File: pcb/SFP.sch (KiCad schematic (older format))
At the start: 13 parts, among them J1101 SFP_CONN

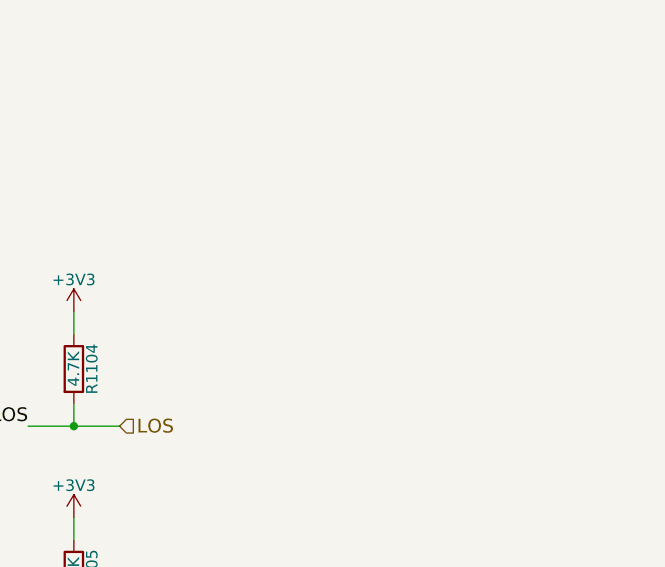
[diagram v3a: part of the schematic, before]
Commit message: Finished most of the routing, removed DDR-3
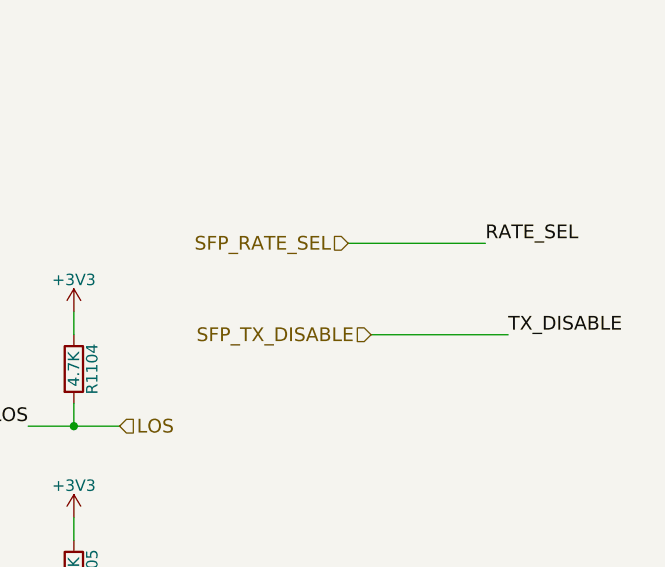
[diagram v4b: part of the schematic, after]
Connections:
- net RATE_SEL renamed SFP_RATE_SEL
- net TX_DISABLE renamed SFP_TX_DISABLE
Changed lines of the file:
@@
 $Descr A4 11693 8268
 encoding utf-8
-Sheet 11 13
+Sheet 9 11
 Title ""
 Date ""
@@
 $EndComp
 $Comp
-L GND #PWR0153
+L GND #PWR0138
 U 1 1 56515F98
 P 2700 3100
-F 0 "#PWR0153" H 2700 2850 50  0001 C CNN
+F 0 "#PWR0138" H 2700 2850 50  0001 C CNN
 F 1 "GND" H 2700 2950 50  0000 C CNN
 F 2 "" H 2700 3100 60  0000 C CNN
@@
 $EndComp
 $Comp
-L +3V3 #PWR0154
+L +3V3 #PWR0139
 U 1 1 56515FAF
 P 7900 1000
-F 0 "#PWR0154" H 7900 850 50  0001 C CNN
+F 0 "#PWR0139" H 7900 850 50  0001 C CNN
 F 1 "+3V3" H 7900 1140 50  0000 C CNN
 F 2 "" H 7900 1000 60  0000 C CNN
@@
 $EndComp
 $Comp
-L GND #PWR0155
+L GND #PWR0140
 U 1 1 56515FCB
 P 7900 1500
-F 0 "#PWR0155" H 7900 1250 50  0001 C CNN
+F 0 "#PWR0140" H 7900 1250 50  0001 C CNN
 F 1 "GND" H 7900 1350 50  0000 C CNN
 F 2 "" H 7900 1500 60  0000 C CNN
@@
 $EndComp
 $Comp
-L GND #PWR0156
+L GND #PWR0141
 U 1 1 565162BE
 P 7000 1500
-F 0 "#PWR0156" H 7000 1250 50  0001 C CNN
+F 0 "#PWR0141" H 7000 1250 50  0001 C CNN
 F 1 "GND" H 7000 1350 50  0000 C CNN
 F 2 "" H 7000 1500 60  0000 C CNN
@@
 $EndComp
 $Comp
-L GND #PWR0157
+L GND #PWR0142
 U 1 1 5651631D
 P 6700 2600
-F 0 "#PWR0157" H 6700 2350 50  0001 C CNN
+F 0 "#PWR0142" H 6700 2350 50  0001 C CNN
 F 1 "GND" H 6700 2450 50  0000 C CNN
 F 2 "" H 6700 2600 60  0000 C CNN
@@
 $EndComp
 $Comp
-L +3V3 #PWR0158
+L +3V3 #PWR0143
 U 1 1 56516349
 P 5700 800
-F 0 "#PWR0158" H 5700 650 50  0001 C CNN
+F 0 "#PWR0143" H 5700 650 50  0001 C CNN
 F 1 "+3V3" H 5700 940 50  0000 C CNN
 F 2 "" H 5700 800 60  0000 C CNN
@@
 $EndComp
 $Comp
-L +3V3 #PWR0159
+L +3V3 #PWR0144
 U 1 1 56516375
 P 5700 1900
-F 0 "#PWR0159" H 5700 1750 50  0001 C CNN
+F 0 "#PWR0144" H 5700 1750 50  0001 C CNN
 F 1 "+3V3" H 5700 2040 50  0000 C CNN
 F 2 "" H 5700 1900 60  0000 C CNN
@@
 $EndComp
 $Comp
-L +3V3 #PWR0160
+L +3V3 #PWR0145
 U 1 1 56516B32
 P 7500 3600
-F 0 "#PWR0160" H 7500 3450 50  0001 C CNN
+F 0 "#PWR0145" H 7500 3450 50  0001 C CNN
 F 1 "+3V3" H 7500 3740 50  0000 C CNN
 F 2 "" H 7500 3600 60  0000 C CNN
@@
 $EndComp
 $Comp
-L +3V3 #PWR0161
+L +3V3 #PWR0146
 U 1 1 56516C8D
 P 7500 4500
-F 0 "#PWR0161" H 7500 4350 50  0001 C CNN
+F 0 "#PWR0146" H 7500 4350 50  0001 C CNN
 F 1 "+3V3" H 7500 4640 50  0000 C CNN
 F 2 "" H 7500 4500 60  0000 C CNN
@@
 $EndComp
 $Comp
-L +3V3 #PWR0162
+L +3V3 #PWR0147
 U 1 1 56516D11
 P 5300 3600
-F 0 "#PWR0162" H 5300 3450 50  0001 C CNN
+F 0 "#PWR0147" H 5300 3450 50  0001 C CNN
 F 1 "+3V3" H 5300 3740 50  0000 C CNN
 F 2 "" H 5300 3600 60  0000 C CNN
@@
 $EndComp
 $Comp
-L +3V3 #PWR0163
+L +3V3 #PWR0148
 U 1 1 56516D21
 P 5300 4500
-F 0 "#PWR0163" H 5300 4350 50  0001 C CNN
+F 0 "#PWR0148" H 5300 4350 50  0001 C CNN
 F 1 "+3V3" H 5300 4640 50  0000 C CNN
 F 2 "" H 5300 4500 60  0000 C CNN
@@
 $EndComp
 $Comp
-L +3V3 #PWR0164
+L +3V3 #PWR0149
 U 1 1 56516DA0
 P 5300 5400
-F 0 "#PWR0164" H 5300 5250 50  0001 C CNN
+F 0 "#PWR0149" H 5300 5250 50  0001 C CNN
 F 1 "+3V3" H 5300 5540 50  0000 C CNN
 F 2 "" H 5300 5400 60  0000 C CNN
@@
 Text HLabel 7700 6000 2    60   Input ~ 0
 SFP_TX_N
+Wire Wire Line
+	8700 3300 9300 3300
+Text HLabel 8700 3300 0    60   Input ~ 0
+SFP_RATE_SEL
+Text Label 9300 3300 0    60   ~ 0
+RATE_SEL
+Text Label 9400 3700 0    60   ~ 0
+TX_DISABLE
+Wire Wire Line
+	9400 3700 8800 3700
+Text HLabel 8800 3700 0    60   Input ~ 0
+SFP_TX_DISABLE
 $EndSCHEMATC

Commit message: Pending final check
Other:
- note added: "SFP has internal AC coupling caps"
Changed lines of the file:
@@
 $EndComp
 $Comp
-L GND #PWR0138
+L GND #PWR0139
 U 1 1 56515F98
 P 2700 3100
-F 0 "#PWR0138" H 2700 2850 50  0001 C CNN
+F 0 "#PWR0139" H 2700 2850 50  0001 C CNN
 F 1 "GND" H 2700 2950 50  0000 C CNN
 F 2 "" H 2700 3100 60  0000 C CNN
@@
 $EndComp
 $Comp
-L +3V3 #PWR0139
+L +3V3 #PWR0140
 U 1 1 56515FAF
 P 7900 1000
-F 0 "#PWR0139" H 7900 850 50  0001 C CNN
+F 0 "#PWR0140" H 7900 850 50  0001 C CNN
 F 1 "+3V3" H 7900 1140 50  0000 C CNN
 F 2 "" H 7900 1000 60  0000 C CNN
@@
 $EndComp
 $Comp
-L GND #PWR0140
+L GND #PWR0141
 U 1 1 56515FCB
 P 7900 1500
-F 0 "#PWR0140" H 7900 1250 50  0001 C CNN
+F 0 "#PWR0141" H 7900 1250 50  0001 C CNN
 F 1 "GND" H 7900 1350 50  0000 C CNN
 F 2 "" H 7900 1500 60  0000 C CNN
@@
 $EndComp
 $Comp
-L GND #PWR0141
+L GND #PWR0142
 U 1 1 565162BE
 P 7000 1500
-F 0 "#PWR0141" H 7000 1250 50  0001 C CNN
+F 0 "#PWR0142" H 7000 1250 50  0001 C CNN
 F 1 "GND" H 7000 1350 50  0000 C CNN
 F 2 "" H 7000 1500 60  0000 C CNN
@@
 $EndComp
 $Comp
-L GND #PWR0142
+L GND #PWR0143
 U 1 1 5651631D
 P 6700 2600
-F 0 "#PWR0142" H 6700 2350 50  0001 C CNN
+F 0 "#PWR0143" H 6700 2350 50  0001 C CNN
 F 1 "GND" H 6700 2450 50  0000 C CNN
 F 2 "" H 6700 2600 60  0000 C CNN
@@
 $EndComp
 $Comp
-L +3V3 #PWR0143
+L +3V3 #PWR0144
 U 1 1 56516349
 P 5700 800
-F 0 "#PWR0143" H 5700 650 50  0001 C CNN
+F 0 "#PWR0144" H 5700 650 50  0001 C CNN
 F 1 "+3V3" H 5700 940 50  0000 C CNN
 F 2 "" H 5700 800 60  0000 C CNN
@@
 $EndComp
 $Comp
-L +3V3 #PWR0144
+L +3V3 #PWR0145
 U 1 1 56516375
 P 5700 1900
-F 0 "#PWR0144" H 5700 1750 50  0001 C CNN
+F 0 "#PWR0145" H 5700 1750 50  0001 C CNN
 F 1 "+3V3" H 5700 2040 50  0000 C CNN
 F 2 "" H 5700 1900 60  0000 C CNN
@@
 $EndComp
 $Comp
-L +3V3 #PWR0145
+L +3V3 #PWR0146
 U 1 1 56516B32
 P 7500 3600
-F 0 "#PWR0145" H 7500 3450 50  0001 C CNN
+F 0 "#PWR0146" H 7500 3450 50  0001 C CNN
 F 1 "+3V3" H 7500 3740 50  0000 C CNN
 F 2 "" H 7500 3600 60  0000 C CNN
@@
 $EndComp
 $Comp
-L +3V3 #PWR0146
+L +3V3 #PWR0147
 U 1 1 56516C8D
 P 7500 4500
-F 0 "#PWR0146" H 7500 4350 50  0001 C CNN
+F 0 "#PWR0147" H 7500 4350 50  0001 C CNN
 F 1 "+3V3" H 7500 4640 50  0000 C CNN
 F 2 "" H 7500 4500 60  0000 C CNN
@@
 $EndComp
 $Comp
-L +3V3 #PWR0147
+L +3V3 #PWR0148
 U 1 1 56516D11
 P 5300 3600
-F 0 "#PWR0147" H 5300 3450 50  0001 C CNN
+F 0 "#PWR0148" H 5300 3450 50  0001 C CNN
 F 1 "+3V3" H 5300 3740 50  0000 C CNN
 F 2 "" H 5300 3600 60  0000 C CNN
@@
 $EndComp
 $Comp
-L +3V3 #PWR0148
+L +3V3 #PWR0149
 U 1 1 56516D21
 P 5300 4500
-F 0 "#PWR0148" H 5300 4350 50  0001 C CNN
+F 0 "#PWR0149" H 5300 4350 50  0001 C CNN
 F 1 "+3V3" H 5300 4640 50  0000 C CNN
 F 2 "" H 5300 4500 60  0000 C CNN
@@
 $EndComp
 $Comp
-L +3V3 #PWR0149
+L +3V3 #PWR0150
 U 1 1 56516DA0
 P 5300 5400
-F 0 "#PWR0149" H 5300 5250 50  0001 C CNN
+F 0 "#PWR0150" H 5300 5250 50  0001 C CNN
 F 1 "+3V3" H 5300 5540 50  0000 C CNN
 F 2 "" H 5300 5400 60  0000 C CNN
@@
 Text HLabel 8800 3700 0    60   Input ~ 0
 SFP_TX_DISABLE
+Text Notes 2650 3750 0    60   ~ 0
+SFP has internal AC coupling caps
 $EndSCHEMATC
